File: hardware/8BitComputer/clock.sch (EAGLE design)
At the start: 29 parts, among them IC1 LM555CN, J1 Power, J2 Power, J3 CLK_OUTS, Q1 P2N2222AZL1G, Q2 P2N2222AZL1G

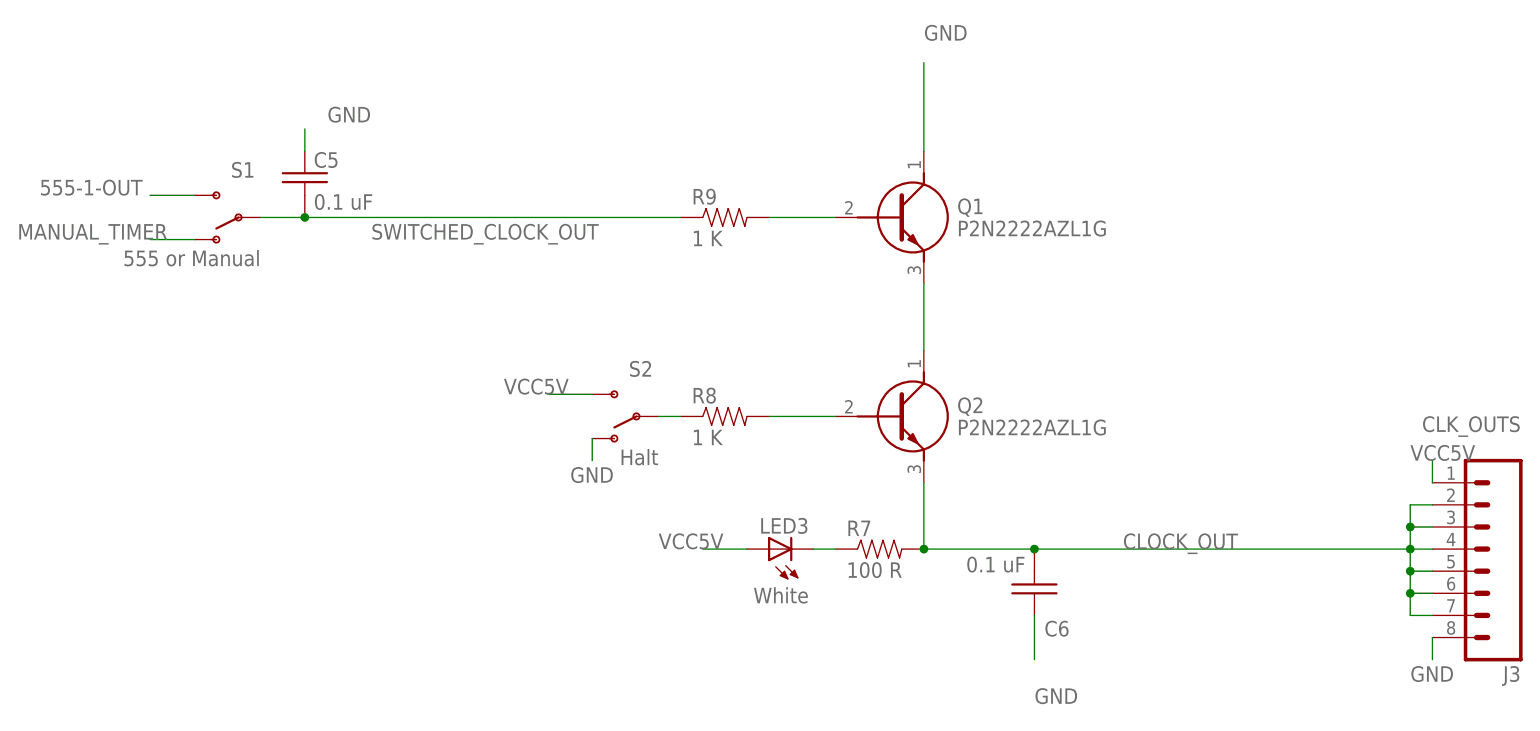
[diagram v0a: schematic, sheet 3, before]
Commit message: fixed clock module so it should actually work now
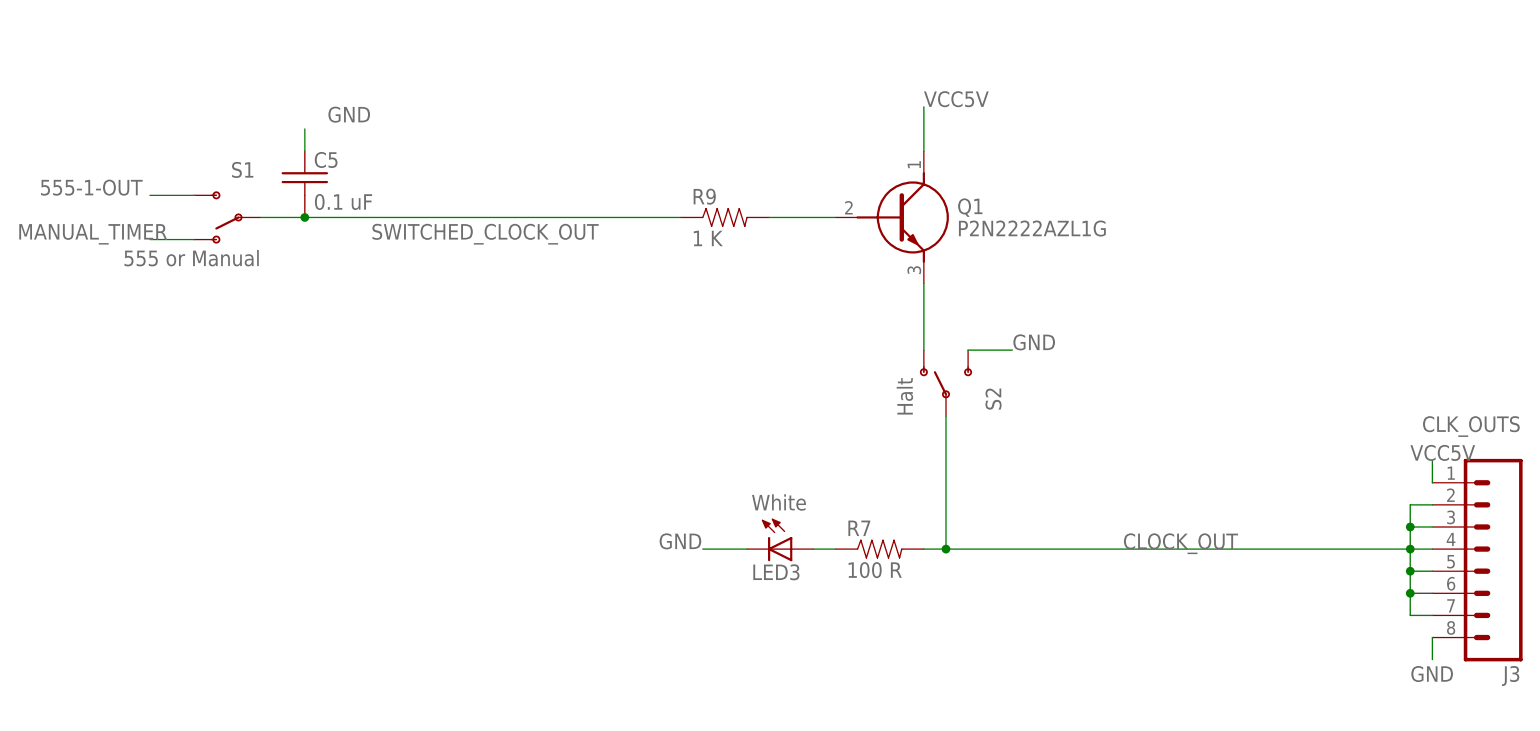
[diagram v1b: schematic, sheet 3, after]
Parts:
- removed C6: 0.1 uF, passives:C-USC0805
- removed Q2: P2N2222AZL1G, transitors:P2N2222AZL1G
- removed R8: 1 K, passives:RESISTOR0805-RES
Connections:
- removed net N$8: R8.1, S2.P
- removed net N$9: Q2.B, R8.2
- net CLOCK_OUT: now also S2.P; no longer C6.2, Q2.E
- net GND: now also LED3.C, S2.S; no longer C6.1, Q1.C, S2.O
- net N$10: now also S2.O; no longer Q2.C
- net N$7: now also LED3.A; no longer LED3.C
- net VCC5V: now also Q1.C; no longer LED3.A, S2.S
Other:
- moved on the sheet: LED3, S2
